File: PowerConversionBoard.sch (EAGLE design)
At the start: 1 part, among them IC1 4002D

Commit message: preliminary crap
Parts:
- removed IC1: 4002D, 40xx:4002D
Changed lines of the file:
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@@
 </classes>
 <parts>
-<part name="IC1" library="40xx" library_urn="urn:adsk.eagle:library:80" deviceset="4002" device="D" package3d_urn="urn:adsk.eagle:package:823/2"/>
+<part name="FRAME1" library="frames" library_urn="urn:adsk.eagle:library:229" deviceset="A3L-LOC" device=""/>
+<part name="FRAME2" library="frames" library_urn="urn:adsk.eagle:library:229" deviceset="A3L-LOC" device=""/>
+<part name="FRAME3" library="frames" library_urn="urn:adsk.eagle:library:229" deviceset="A3L-LOC" device=""/>
 </parts>
 <sheets>
@@
 </plain>
 <instances>
-<instance part="IC1" gate="A" x="27.94" y="55.88" smashed="yes">
-<attribute name="NAME" x="31.75" y="60.96" size="1.778" layer="95"/>
-<attribute name="VALUE" x="31.75" y="48.895" size="1.778" layer="96"/>
+<instance part="FRAME1" gate="G$1" x="-157.48" y="-116.84" smashed="yes">
+<attribute name="DRAWING_NAME" x="186.69" y="-101.6" size="2.54" layer="94"/>
+<attribute name="LAST_DATE_TIME" x="186.69" y="-106.68" size="2.286" layer="94"/>
+<attribute name="SHEET" x="200.025" y="-111.76" size="2.54" layer="94"/>
+</instance>
+<instance part="FRAME2" gate="G$1" x="246.38" y="-116.84" smashed="yes">
+<attribute name="DRAWING_NAME" x="590.55" y="-101.6" size="2.54" layer="94"/>
+<attribute name="LAST_DATE_TIME" x="590.55" y="-106.68" size="2.286" layer="94"/>
+<attribute name="SHEET" x="603.885" y="-111.76" size="2.54" layer="94"/>
+</instance>
+<instance part="FRAME3" gate="G$1" x="-157.48" y="-391.16" smashed="yes">
+<attribute name="DRAWING_NAME" x="186.69" y="-375.92" size="2.54" layer="94"/>
+<attribute name="LAST_DATE_TIME" x="186.69" y="-381" size="2.286" layer="94"/>
+<attribute name="SHEET" x="200.025" y="-386.08" size="2.54" layer="94"/>
 </instance>
 </instances>
@@
 will not be understood (or retained) with this version.
 </note>
-<note version="8.3" severity="warning">
-Since Version 8.3, EAGLE supports the association of 3D packages
-with devices in libraries, schematics, and board files. Those 3D
-packages will not be understood (or retained) with this version.
-</note>
 </compatibility>

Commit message: fixing local copy
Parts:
- added C10, C11, C12, C24, C25, C26: 150uF, PowerComponents:C-TANTALUM(10UF_150UF)
- added C14, C15, C16, C17, C18, C29, C30, C31: 10uF, PowerComponents:C-TANTALUM(10UF_150UF)
- added C20, C6: 10nF, SparkFun-Capacitors:10NF-0603-50V-10%
- added C3, C7: 0.47uF, rcl:C-EUC0603
- added C32: 100uF, Seeed-Capacitor:TANTALUM-SMD-10UF-16V-10%(AVX-A)
- added C33: 10uF, Seeed-Capacitor:TANTALUM-SMD-10UF-16V-10%(AVX-A)
- added C34: .1uF, Seeed-Capacitor:TANTALUM-SMD-10UF-16V-10%(AVX-A)
- added C35: .01uF, Seeed-Capacitor:TANTALUM-SMD-10UF-16V-10%(AVX-A)
- added J1, J2, J4, J5, J6: (no value), SparkFun-Connectors:BANANA_CONN
- added R3: 10k, SparkFun-Resistors:10KOHM-0603-1/10W-1%
- added R4: 1.2 ohms, SparkFun-Resistors:RESISTOR0603
- added R6: 0, audio amplifier example:R-US_R1206
- added U$1, U$3: SWITCHMODE_SCHOTTKY, PowerComponents:SWITCHMODE_SCHOTTKY
- added U$10, U$9: 7.8 uH, DiscreteComponents:HCMA1305
- added U$13: 47 uF, Nordic_nRF:CAPACITOR_0603_N
- added U$4: TO-263, TPS758:TO-263
- added U1, U2: LM2678, PowerComponents:LM2678
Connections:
- new net +12V: C14.+, C15.+, C16.+, C17.+, C18.+, C29.+, C3.1, C30.+, C31.+, C7.1, J1.1, U1.VIN, U2.VIN
- new net +3.3V: J5.1, U$13.1, U$4.OUT
- new net +5V: C10.+, C11.+, C12.+, J6.1, U1.FEEDBACK
- new net +5V_3.3V: C24.+, C25.+, C26.+, U$4.EN, U$4.IN, U$9.2, U2.FEEDBACK
- new net 3.3VGND: C32.-, C33.-, C34.-, C35.-, J4.1, R3.2, R4.1, R6.1, U$10.1, U$3.P$1, U$3.P$3, U$4.GND, U2.GND, U2.TABGND
- new net 5VGND: C10.-, C11.-, C12.-, U$1.P$1, U$1.P$3
- new net GND: C14.-, C15.-, C16.-, C17.-, C18.-, C29.-, C3.2, C30.-, C31.-, C32.+, C33.+, C34.+, C35.+, C7.2, J2.1, R3.1, U1.GND, U1.TABGND
- new net N$1: C6.2, U$1.P$4, U1.OUTPUT
- new net N$10: R4.2, U$13.2
- new net N$2: C20.1, U2.BOOST
- new net N$3: C6.1, U1.BOOST
- new net N$4: C24.-, C25.-, C26.-, R6.2, U$10.2
- new net N$7: C20.2, U$3.P$4, U$9.1, U2.OUTPUT

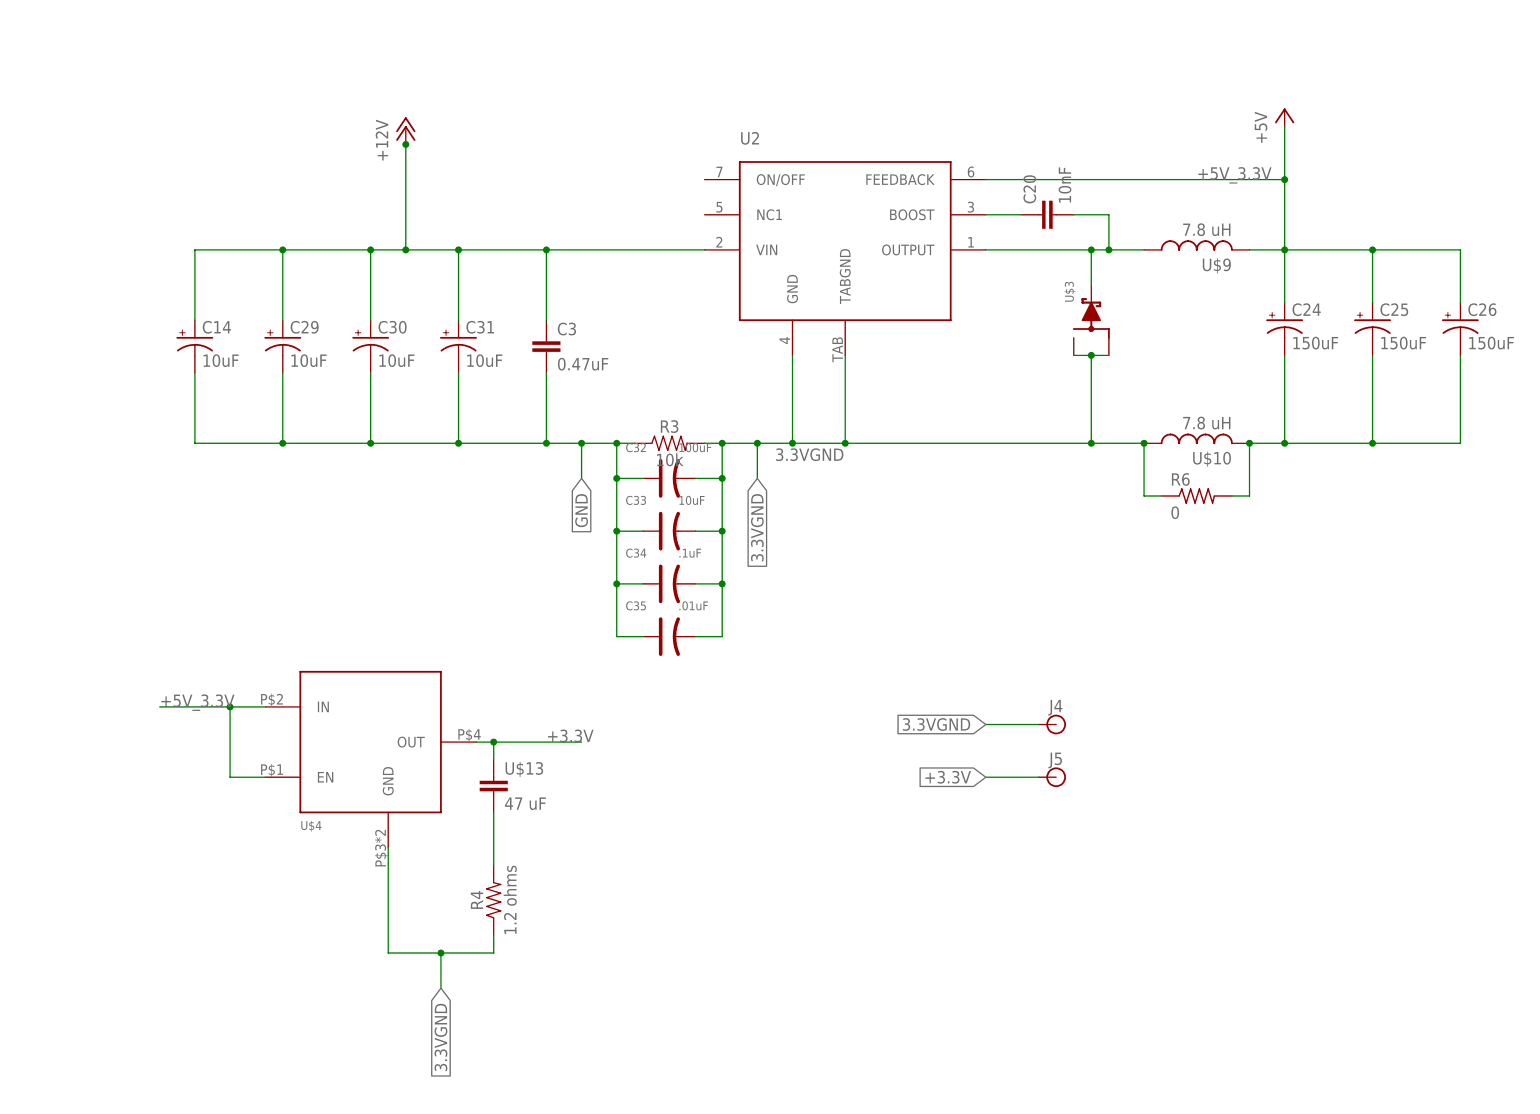
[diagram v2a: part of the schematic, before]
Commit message: Grid size changed to 0.01 in - same as last years
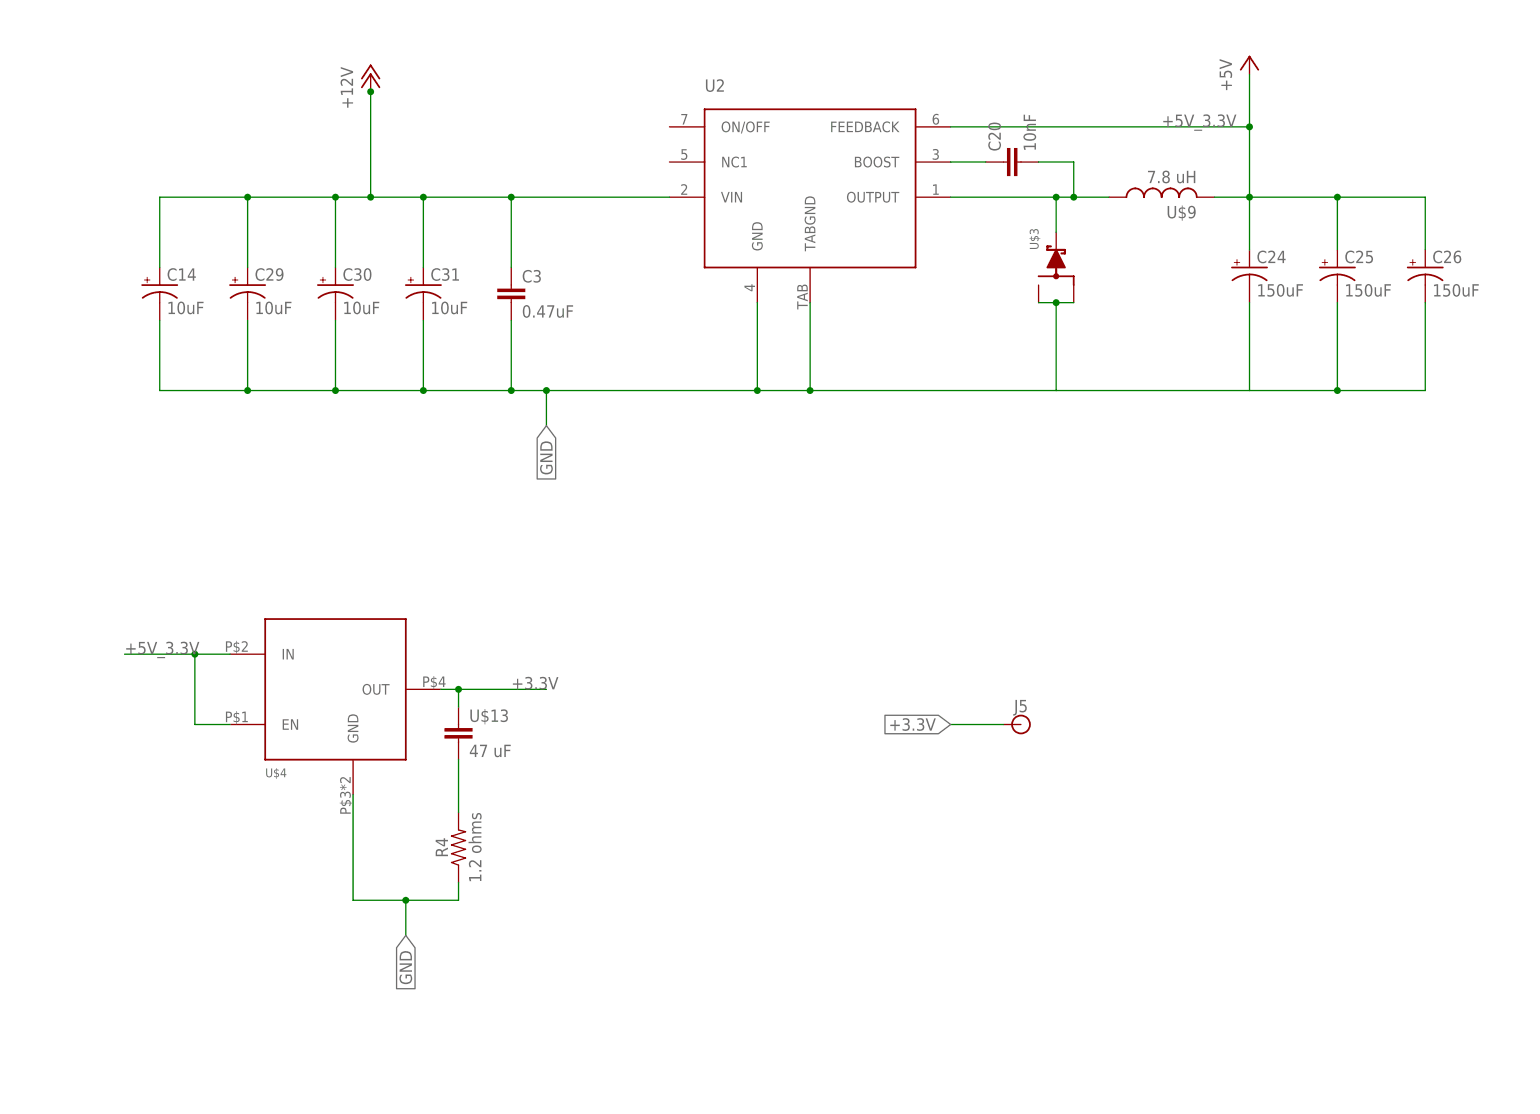
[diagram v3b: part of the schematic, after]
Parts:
- removed C32: 100uF, Seeed-Capacitor:TANTALUM-SMD-10UF-16V-10%(AVX-A)
- removed C33: 10uF, Seeed-Capacitor:TANTALUM-SMD-10UF-16V-10%(AVX-A)
- removed C34: .1uF, Seeed-Capacitor:TANTALUM-SMD-10UF-16V-10%(AVX-A)
- removed C35: .01uF, Seeed-Capacitor:TANTALUM-SMD-10UF-16V-10%(AVX-A)
- removed J4: (no value), SparkFun-Connectors:BANANA_CONN
- removed R3: 10k, SparkFun-Resistors:10KOHM-0603-1/10W-1%
- removed R6: 0, audio amplifier example:R-US_R1206
- removed U$10: 7.8 uH, DiscreteComponents:HCMA1305
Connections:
- removed net 3.3VGND: C32.-, C33.-, C34.-, C35.-, J4.1, R3.2, R4.1, R6.1, U$10.1, U$3.P$1, U$3.P$3, U$4.GND, U2.GND, U2.TABGND
- removed net N$4: C24.-, C25.-, C26.-, R6.2, U$10.2
- net GND: now also C24.-, C25.-, C26.-, R4.1, U$3.P$1, U$3.P$3, U$4.GND, U2.GND, U2.TABGND; no longer C32.+, C33.+, C34.+, C35.+, R3.1
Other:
- moved on the sheet: C14, C20, C24, C25, C26, C29, C3, C30, C31, J5, R4, U$13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

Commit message: saving changes
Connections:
- removed net 5VGND: C10.-, C11.-, C12.-, U$1.P$1, U$1.P$3
- net GND: now also C10.-, C11.-, C12.-, U$1.P$1, U$1.P$3
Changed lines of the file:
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@@
 <pinref part="C18" gate="G$1" pin="-"/>
 <pinref part="C7" gate="G$1" pin="2"/>
+<pinref part="U$1" gate="G$1" pin="P$1"/>
+<pinref part="U$1" gate="G$1" pin="P$3"/>
+<wire x1="35.052" y1="56.134" x2="37.592" y2="56.134" width="0.1524" layer="91"/>
+<wire x1="37.592" y1="56.134" x2="40.132" y2="56.134" width="0.1524" layer="91"/>
+<wire x1="37.592" y1="56.134" x2="37.592" y2="43.434" width="0.1524" layer="91"/>
+<junction x="37.592" y="56.134"/>
+<junction x="37.592" y="43.434"/>
+<wire x1="93.472" y1="43.434" x2="80.772" y2="43.434" width="0.1524" layer="91"/>
+<wire x1="80.772" y1="43.434" x2="68.072" y2="43.434" width="0.1524" layer="91"/>
+<pinref part="C10" gate="G$1" pin="-"/>
+<wire x1="68.072" y1="56.134" x2="68.072" y2="43.434" width="0.1524" layer="91"/>
+<junction x="68.072" y="43.434"/>
+<pinref part="C11" gate="G$1" pin="-"/>
+<wire x1="80.772" y1="56.134" x2="80.772" y2="43.434" width="0.1524" layer="91"/>
+<junction x="80.772" y="43.434"/>
+<pinref part="C12" gate="G$1" pin="-"/>
+<wire x1="93.472" y1="56.134" x2="93.472" y2="43.434" width="0.1524" layer="91"/>
+<wire x1="37.592" y1="43.434" x2="68.072" y2="43.434" width="0.1524" layer="91"/>
+<wire x1="37.592" y1="43.434" x2="7.112" y2="43.434" width="0.1524" layer="91"/>
+<junction x="7.112" y="43.434"/>
+<wire x1="7.112" y1="43.434" x2="4.826" y2="43.434" width="0.1524" layer="91"/>
 </segment>
 <segment>
@@
 </segment>
 </net>
-<net name="5VGND" class="0">
-<segment>
-<pinref part="U$1" gate="G$1" pin="P$1"/>
-<pinref part="U$1" gate="G$1" pin="P$3"/>
-<wire x1="35.052" y1="56.134" x2="37.592" y2="56.134" width="0.1524" layer="91"/>
-<wire x1="37.592" y1="56.134" x2="40.132" y2="56.134" width="0.1524" layer="91"/>
-<wire x1="37.592" y1="56.134" x2="37.592" y2="43.434" width="0.1524" layer="91"/>
-<junction x="37.592" y="56.134"/>
-<junction x="37.592" y="43.434"/>
-<wire x1="93.472" y1="43.434" x2="80.772" y2="43.434" width="0.1524" layer="91"/>
-<wire x1="80.772" y1="43.434" x2="68.072" y2="43.434" width="0.1524" layer="91"/>
-<pinref part="C10" gate="G$1" pin="-"/>
-<wire x1="68.072" y1="56.134" x2="68.072" y2="43.434" width="0.1524" layer="91"/>
-<junction x="68.072" y="43.434"/>
-<pinref part="C11" gate="G$1" pin="-"/>
-<wire x1="80.772" y1="56.134" x2="80.772" y2="43.434" width="0.1524" layer="91"/>
-<junction x="80.772" y="43.434"/>
-<pinref part="C12" gate="G$1" pin="-"/>
-<wire x1="93.472" y1="56.134" x2="93.472" y2="43.434" width="0.1524" layer="91"/>
-<wire x1="37.592" y1="43.434" x2="68.072" y2="43.434" width="0.1524" layer="91"/>
-<wire x1="37.592" y1="43.434" x2="4.826" y2="43.434" width="0.1524" layer="91"/>
-</segment>
-</net>

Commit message: Good Inductor
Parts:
- removed U$9: 7.8 uH, DiscreteComponents:HCMA1305
- added U$2, U$5: HCM1305, HCM1305:HCM1305
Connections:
- net +5V: now also U$5.2
- net +5V_3.3V: now also U$2.2; no longer U$9.2
- net N$1: now also U$5.1
- net N$7: now also U$2.1; no longer U$9.1
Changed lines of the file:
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@@
 <part name="U$4" library="TPS758" deviceset="TO-263" device=""/>
 <part name="R4" library="SparkFun-Resistors" library_urn="urn:adsk.eagle:library:532" deviceset="RESISTOR" device="0603" package3d_urn="urn:adsk.eagle:package:39650/1" value=" 1.2 ohms"/>
-<part name="U$9" library="DiscreteComponents" deviceset="HCMA1305" device="" value="7.8 uH"/>
 <part name="J5" library="SparkFun-Connectors" library_urn="urn:adsk.eagle:library:513" deviceset="BANANA_CONN" device="" package3d_urn="urn:adsk.eagle:package:38018/1"/>
 <part name="C14" library="PowerComponents" deviceset="C-TANTALUM(10UF_150UF)" device="" value="10uF"/>
@@
 <part name="C26" library="PowerComponents" deviceset="C-TANTALUM(10UF_150UF)" device="" value="150uF"/>
 <part name="U$13" library="Nordic_nRF" library_urn="urn:adsk.eagle:library:169009" deviceset="CAPACITOR" device="_0603_N" package3d_urn="urn:adsk.eagle:package:2593734/1" value="47 uF"/>
+<part name="U$2" library="HCM1305" deviceset="HCM1305" device=""/>
+<part name="U$5" library="HCM1305" deviceset="HCM1305" device=""/>
 </parts>
 <sheets>
@@
 <attribute name="VALUE" x="376.682" y="-27.94" size="1.778" layer="96" font="vector" rot="R90" align="top-center"/>
 </instance>
-<instance part="U$9" gate="G$1" x="476.758" y="66.04" smashed="yes" rot="R90">
-<attribute name="NAME" x="481.838" y="64.77" size="1.778" layer="95" rot="R180"/>
-<attribute name="VALUE" x="481.838" y="69.85" size="1.778" layer="96" rot="R180"/>
-</instance>
 <instance part="J5" gate="G$1" x="456.438" y="-10.16" smashed="yes">
 <attribute name="NAME" x="455.422" y="-8.382" size="1.778" layer="95" font="vector"/>
@@
 <attribute name="NAME" x="376.682" y="-9.779" size="1.778" layer="95"/>
 <attribute name="VALUE" x="376.682" y="-14.859" size="1.778" layer="96"/>
+</instance>
+<instance part="U$2" gate="G$1" x="476.758" y="66.04" smashed="yes" rot="R90">
+<attribute name="NAME" x="471.66238125" y="68.587809375" size="1.78346875" layer="95"/>
+</instance>
+<instance part="U$5" gate="G$1" x="52.832" y="71.374" smashed="yes" rot="R90">
+<attribute name="NAME" x="47.73638125" y="73.921809375" size="1.78346875" layer="95"/>
 </instance>
 </instances>
@@
 <pinref part="C12" gate="G$1" pin="+"/>
 <wire x1="93.472" y1="63.754" x2="93.472" y2="71.374" width="0.1524" layer="91"/>
+<pinref part="U$5" gate="G$1" pin="2"/>
 </segment>
 <segment>
@@
 <wire x1="37.592" y1="66.294" x2="37.592" y2="71.374" width="0.1524" layer="91"/>
 <junction x="37.592" y="71.374"/>
+<pinref part="U$5" gate="G$1" pin="1"/>
 </segment>
 </net>
@@
 <wire x1="461.518" y1="60.96" x2="461.518" y2="66.04" width="0.1524" layer="91"/>
 <junction x="461.518" y="66.04"/>
-<pinref part="U$9" gate="G$1" pin="1"/>
+<pinref part="U$2" gate="G$1" pin="1"/>
 </segment>
 </net>
@@
 <junction x="489.458" y="76.2"/>
 <label x="476.758" y="76.2" size="1.778" layer="95"/>
-<pinref part="U$9" gate="G$1" pin="2"/>
 <pinref part="C24" gate="G$1" pin="+"/>
 <wire x1="489.458" y1="58.42" x2="489.458" y2="66.04" width="0.1524" layer="91"/>
@@
 <pinref part="C26" gate="G$1" pin="+"/>
 <wire x1="514.858" y1="58.42" x2="514.858" y2="66.04" width="0.1524" layer="91"/>
-</segment>
-<segment>
+<pinref part="U$2" gate="G$1" pin="2"/>
+</segment>
+<segment>

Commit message: note
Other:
- note added: "Insert LEDs 470 ohm maybe for the 12v 5_3v 5v 3v rails"
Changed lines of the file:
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@@
 <sheet>
 <plain>
+<text x="34.036" y="27.178" size="1.778" layer="91">Insert LEDs 470 ohm maybe for the 12v 5_3v 5v 3v rails </text>
 </plain>
 <instances>
